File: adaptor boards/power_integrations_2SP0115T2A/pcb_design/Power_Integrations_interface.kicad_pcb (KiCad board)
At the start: 2 copper layers, 160 x 90 mm, 1042 parts, among them J1 GATE_DRIVER_CONN_U, J10 current sensor, J2 GATE_DRIVER_CONN_V, J3 GATE_DRIVER_CONN_W, J4 VBUS, J5 CONN-100MIL-F-1x2, J6 CONN-100MIL-M-1x4, J8 current sensor, J9 current sensor, P1 2SP0115T_conector, P2 2SP0115T_conector, P3 2SP0115T_conector, T1 TRANS-2CT, T2 TRANS-2CT, U1 LM1117IMP-v.v, U12 AMC1301, U2 SN6501DBV, U3 AMC1301, U4 TPS76350, U5 SN6501DBV, U6 AMC1301, U7 TPS76350, U9 AMC1301

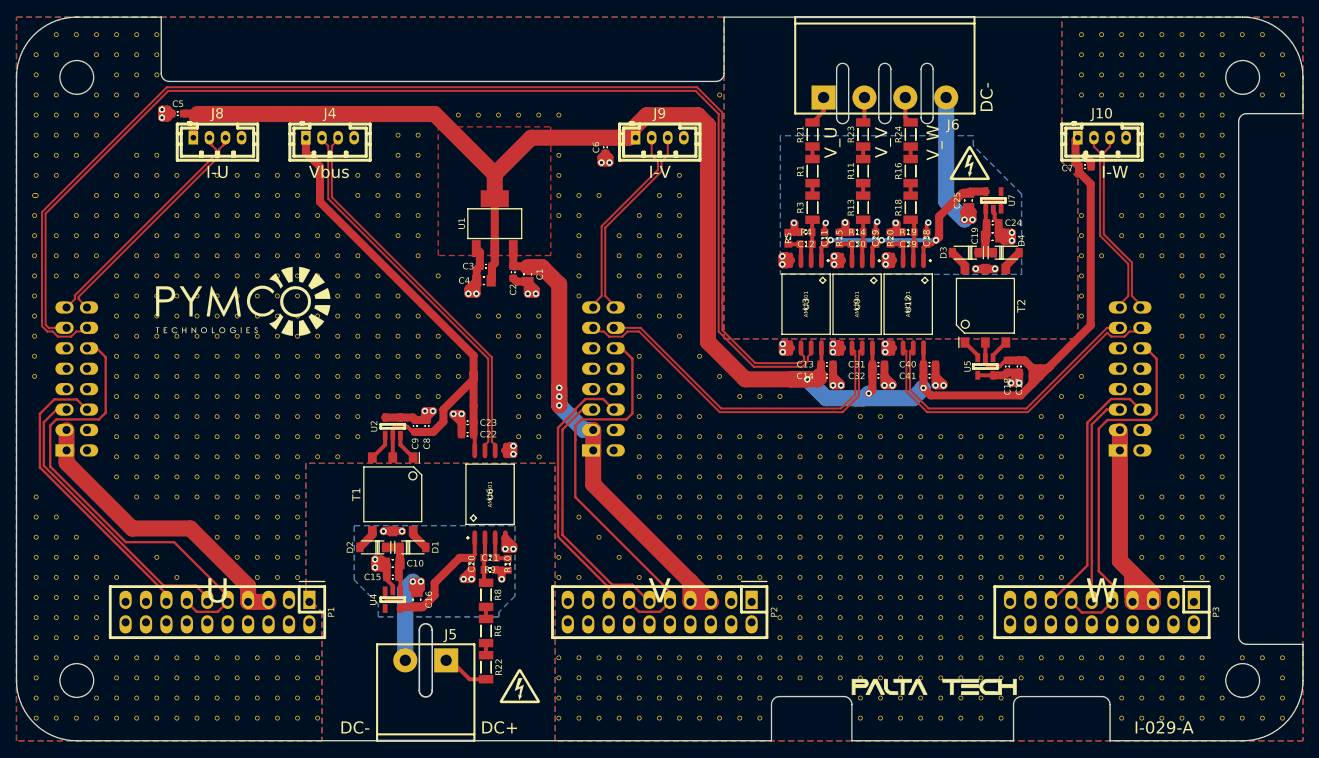
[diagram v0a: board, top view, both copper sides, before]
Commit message: Fix swapped differential signals in the interface board
Signed-off-by: Marcos Chaparro <mchaparro@paltatech.com>
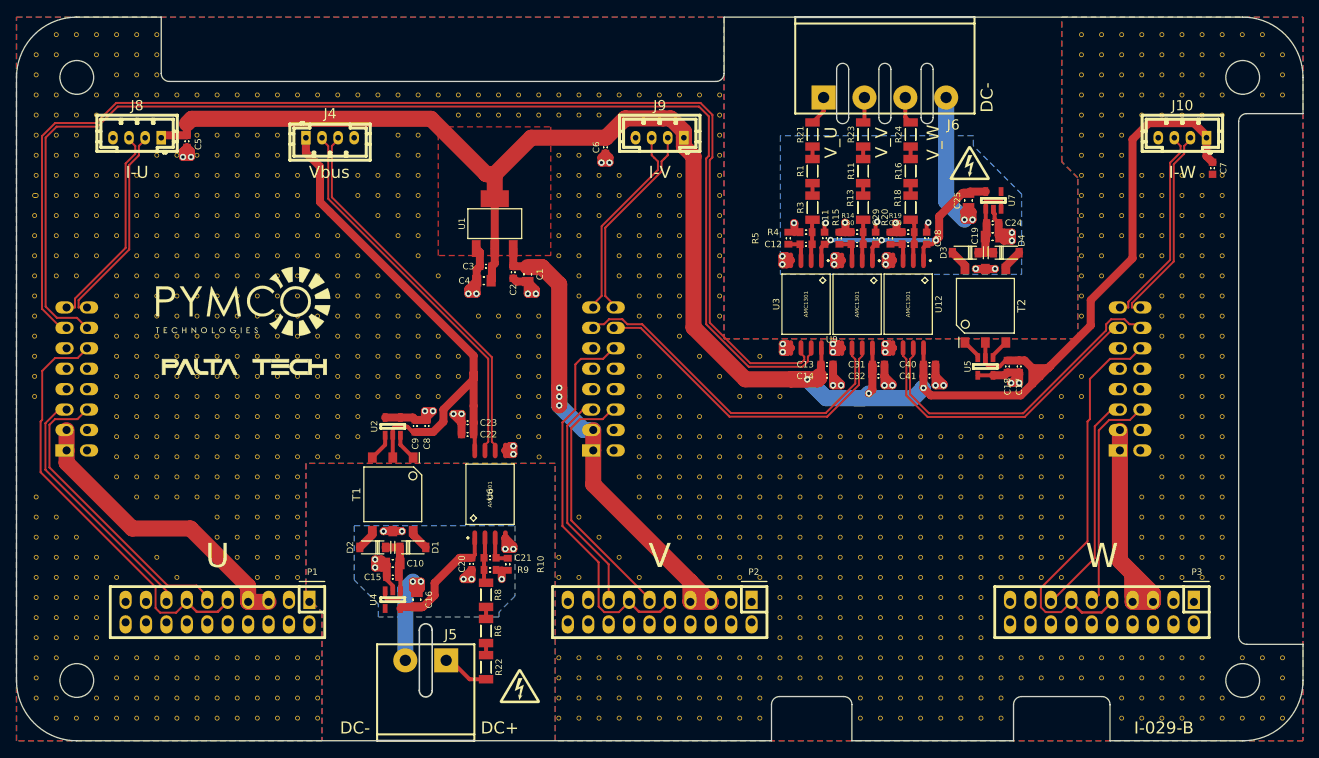
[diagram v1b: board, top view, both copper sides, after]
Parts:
- removed V1_35, V4_6, V5_5, V60_7, V6_7: AUTO_VIA, VIA_MATRIX
- added V10_17: AUTO_VIA, VIA_MATRIX, F.Cu at (-50.0, -35.3)
- added V10_17: AUTO_VIA, VIA_MATRIX, F.Cu at (-25.0, -35.3)
- added V10_8: AUTO_VIA, VIA_MATRIX, F.Cu at (-55.0, -30.3)
- added V10_9: AUTO_VIA, VIA_MATRIX, F.Cu at (-55.0, -27.8)
- added V11_17: AUTO_VIA, VIA_MATRIX, F.Cu at (-47.5, -35.3)
- added V11_17: AUTO_VIA, VIA_MATRIX, F.Cu at (-22.5, -35.3)
- added V11_8: AUTO_VIA, VIA_MATRIX, F.Cu at (-52.5, -30.3)
- added V11_9: AUTO_VIA, VIA_MATRIX, F.Cu at (-52.5, -27.8)
- added V12_17: AUTO_VIA, VIA_MATRIX, F.Cu at (-45.0, -35.3)
- added V12_17: AUTO_VIA, VIA_MATRIX, F.Cu at (-20.0, -35.3)
- added V12_8: AUTO_VIA, VIA_MATRIX, F.Cu at (-50.0, -30.3)
- added V12_9: AUTO_VIA, VIA_MATRIX, F.Cu at (-50.0, -27.8)
- added V13_17: AUTO_VIA, VIA_MATRIX, F.Cu at (-42.5, -35.3)
- added V13_17: AUTO_VIA, VIA_MATRIX, F.Cu at (-17.5, -35.3)
- added V13_8: AUTO_VIA, VIA_MATRIX, F.Cu at (-47.5, -30.3)
- added V13_9: AUTO_VIA, VIA_MATRIX, F.Cu at (-47.5, -27.8)
- added V14_17: AUTO_VIA, VIA_MATRIX, F.Cu at (-40.0, -35.3)
- added V14_17: AUTO_VIA, VIA_MATRIX, F.Cu at (-15.0, -35.3)
- added V15_17: AUTO_VIA, VIA_MATRIX, F.Cu at (-12.5, -35.3)
- added V16_17: AUTO_VIA, VIA_MATRIX, F.Cu at (-10.0, -35.3)
- added V17_17: AUTO_VIA, VIA_MATRIX, F.Cu at (-7.55, -35.3)
- added V18_17: AUTO_VIA, VIA_MATRIX, F.Cu at (-5.05, -35.3)
- added V19_17: AUTO_VIA, VIA_MATRIX, F.Cu at (-2.55, -35.3)
- added V1_8: AUTO_VIA, VIA_MATRIX, F.Cu at (-77.7, 2.18)
- added V20_17: AUTO_VIA, VIA_MATRIX, F.Cu at (-0.05, -35.3)
- added V21_17: AUTO_VIA, VIA_MATRIX, F.Cu at (2.45, -35.3)
- added V22_17: AUTO_VIA, VIA_MATRIX, F.Cu at (4.95, -35.3)
- added V26_5: AUTO_VIA, VIA_MATRIX, F.Cu at (-10.0, -32.8)
- added V27_10: AUTO_VIA, VIA_MATRIX, F.Cu at (-12.5, -15.3)
- added V27_5: AUTO_VIA, VIA_MATRIX, F.Cu at (-7.55, -32.8)
- added V27_7: AUTO_VIA, VIA_MATRIX, F.Cu at (-10.0, -27.8)
- added V27_9: AUTO_VIA, VIA_MATRIX, F.Cu at (-12.5, -17.8)
- added V28_10: AUTO_VIA, VIA_MATRIX, F.Cu at (-7.55, -20.3)
- added V28_9: AUTO_VIA, VIA_MATRIX, F.Cu at (-10.0, -25.3)
- added V29_9: AUTO_VIA, VIA_MATRIX, F.Cu at (-5.05, -25.3)
- added V29_9: AUTO_VIA, VIA_MATRIX, F.Cu at (-5.05, -22.8)
- added V29_9: AUTO_VIA, VIA_MATRIX, F.Cu at (-7.55, -25.3)
- added V2_11: AUTO_VIA, VIA_MATRIX, F.Cu at (-75.0, -20.3)
- added V33_10: AUTO_VIA, VIA_MATRIX, F.Cu at (7.45, -22.8)
- added V33_11: AUTO_VIA, VIA_MATRIX, F.Cu at (7.45, -20.3)
- added V33_12: AUTO_VIA, VIA_MATRIX, F.Cu at (7.45, -17.8)
- added V33_13: AUTO_VIA, VIA_MATRIX, F.Cu at (7.45, -15.3)
- added V33_14: AUTO_VIA, VIA_MATRIX, F.Cu at (7.45, -12.8)
- added V33_15: AUTO_VIA, VIA_MATRIX, F.Cu at (7.45, -10.3)
- added V33_16: AUTO_VIA, VIA_MATRIX, F.Cu at (7.45, -7.82)
- added V33_8: AUTO_VIA, VIA_MATRIX, F.Cu at (7.45, -32.8)
- added V33_8: AUTO_VIA, VIA_MATRIX, F.Cu at (7.45, -27.8)
- added V33_9: AUTO_VIA, VIA_MATRIX, F.Cu at (7.45, -30.3)
- added V33_9: AUTO_VIA, VIA_MATRIX, F.Cu at (7.45, -25.3)
- added V36_19: AUTO_VIA, VIA_MATRIX, F.Cu at (12.5, -2.82)
- added V3_10: AUTO_VIA, VIA_MATRIX, F.Cu at (-75.0, -22.8)
- added V4_10: AUTO_VIA, VIA_MATRIX, F.Cu at (-72.5, -25.3)
- added V4_10: AUTO_VIA, VIA_MATRIX, F.Cu at (-72.5, -22.8)
- added V4_9: AUTO_VIA, VIA_MATRIX, F.Cu at (-70.0, -25.3)
- added V53_4: AUTO_VIA, VIA_MATRIX, F.Cu at (52.5, -27.8)
- added V54_12: AUTO_VIA, VIA_MATRIX, F.Cu at (55.0, -12.8)
- added V54_4: AUTO_VIA, VIA_MATRIX, F.Cu at (55.0, -27.8)
- added V55_4: AUTO_VIA, VIA_MATRIX, F.Cu at (57.5, -27.8)
- added V56_12: AUTO_VIA, VIA_MATRIX, F.Cu at (60.0, -12.8)
- added V57_24: AUTO_VIA, VIA_MATRIX, F.Cu at (62.5, 9.68)
- added V57_25: AUTO_VIA, VIA_MATRIX, F.Cu at (62.5, 12.2)
- added V57_6: AUTO_VIA, VIA_MATRIX, F.Cu at (52.5, -25.3)
- added V57_7: AUTO_VIA, VIA_MATRIX, F.Cu at (52.5, -22.8)
- added V58_14: AUTO_VIA, VIA_MATRIX, F.Cu at (62.5, -10.3)
- added V58_15: AUTO_VIA, VIA_MATRIX, F.Cu at (62.5, -7.82)
- added V58_16: AUTO_VIA, VIA_MATRIX, F.Cu at (62.5, -5.32)
- added V58_6: AUTO_VIA, VIA_MATRIX, F.Cu at (55.0, -20.3)
- added V58_6: AUTO_VIA, VIA_MATRIX, F.Cu at (55.0, -25.3)
- added V58_7: AUTO_VIA, VIA_MATRIX, F.Cu at (55.0, -17.8)
- added V58_7: AUTO_VIA, VIA_MATRIX, F.Cu at (55.0, -22.8)
- added V59_6: AUTO_VIA, VIA_MATRIX, F.Cu at (57.5, -25.3)
- added V59_7: AUTO_VIA, VIA_MATRIX, F.Cu at (57.5, -22.8)
- added V6_12: AUTO_VIA, VIA_MATRIX, F.Cu at (-65.0, -17.8)
- added V6_17: AUTO_VIA, VIA_MATRIX, F.Cu at (-60.0, -35.3)
- added V6_17: AUTO_VIA, VIA_MATRIX, F.Cu at (-62.5, -35.3)
- added V6_17: AUTO_VIA, VIA_MATRIX, F.Cu at (-37.5, -35.3)
- added V6_17: AUTO_VIA, VIA_MATRIX, F.Cu at (-35.0, -35.3)
- added V7_11: AUTO_VIA, VIA_MATRIX, F.Cu at (-62.5, -20.3)
- added V7_17: AUTO_VIA, VIA_MATRIX, F.Cu at (-57.5, -35.3)
- added V7_17: AUTO_VIA, VIA_MATRIX, F.Cu at (-32.5, -35.3)
- added V8_10: AUTO_VIA, VIA_MATRIX, F.Cu at (-60.0, -27.8)
- added V8_10: AUTO_VIA, VIA_MATRIX, F.Cu at (-60.0, -22.8)
- added V8_17: AUTO_VIA, VIA_MATRIX, F.Cu at (-55.0, -35.3)
- added V8_17: AUTO_VIA, VIA_MATRIX, F.Cu at (-30.0, -35.3)
- added V9_17: AUTO_VIA, VIA_MATRIX, F.Cu at (-52.5, -35.3)
- added V9_17: AUTO_VIA, VIA_MATRIX, F.Cu at (-27.5, -35.3)
- added V9_9: AUTO_VIA, VIA_MATRIX, F.Cu at (-57.5, -30.3)
- added V9_9: AUTO_VIA, VIA_MATRIX, F.Cu at (-57.5, -27.8)
- added V9_9: AUTO_VIA, VIA_MATRIX, F.Cu at (-57.5, -25.3)
- C1, C4: value 10uF -> 22uF
- J6: value CONN-100MIL-M-1x4 -> Phoenix 1757268 5.08mm
- R1, R11, R13, R16, R18, R21, R22, R23, R24, R3, R6, R8: value 1M -> 500k
- moved G*** 94.6 mm to (-51.8, -1.50)
- moved C7 15.9 mm to (68.8, -26.2), turned to 270 degrees
- moved V57_6 10.3 mm to (52.5, -32.8)
- moved V57_7 10.3 mm to (52.5, -30.3)
- moved V58_6 10.3 mm to (55.0, -32.8)
- moved V58_7 10.3 mm to (55.0, -30.3)
- moved V59_6 10.3 mm to (57.5, -32.8)
- moved V59_7 10.3 mm to (57.5, -30.3)
- moved V60_6 10.3 mm to (60.0, -32.8)
- moved J10 10.0 mm to (65.0, -30.0), turned to 180 degrees
- moved J8 10.0 mm to (-65.0, -30.0), turned to 180 degrees
- moved C5 3.64 mm to (-58.8, -29.6), turned to 270 degrees
- turned J9 to 180 degrees
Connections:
- J1 pad 13: /V_phase_U/Vout+ -> /V_phase_U/Vout-
- J1 pad 14: /V_phase_U/Vout- -> /V_phase_U/Vout+
- J1 pad 15: /I_phase_U+ -> /I_phase_U-
- J1 pad 16: /I_phase_U- -> /I_phase_U+
- J2 pad 13: /V_phase_V/Vout+ -> /V_phase_V/Vout-
- J2 pad 14: /V_phase_V/Vout- -> /V_phase_V/Vout+
- J2 pad 15: /I_phase_V+ -> /I_phase_V-
- J2 pad 16: /I_phase_V- -> /I_phase_V+
- J3 pad 13: /V_phase_W/Vout+ -> /V_phase_W/Vout-
- J3 pad 14: /V_phase_W/Vout- -> /V_phase_W/Vout+
- J3 pad 15: /I_phase_W+ -> /I_phase_W-
- J3 pad 16: /I_phase_W- -> /I_phase_W+
- P1 pad 11: Net-(J1-Pad5) -> Net-(J1-Pad6)
- P1 pad 15: Net-(J1-Pad6) -> Net-(J1-Pad5)
- P2 pad 11: Net-(J2-Pad5) -> Net-(J2-Pad6)
- P2 pad 15: Net-(J2-Pad6) -> Net-(J2-Pad5)
- P3 pad 11: Net-(J3-Pad5) -> Net-(J3-Pad6)
- P3 pad 15: Net-(J3-Pad6) -> Net-(J3-Pad5)
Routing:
- net +5: track 235.4 -> 244.8 mm
- net /V_phase_U/Vout+: track 149.9 -> 155.4 mm
- net /V_phase_W/Vout+: track 36.6 -> 41.9 mm
- net /I_phase_U+: track 30.4 -> 25.6 mm
- net /I_phase_U-: track 30.3 -> 25.6 mm
- net Net-(J3-Pad6): track 32.5 -> 27.9 mm
- net ~FAULT_W: track 45.8 -> 50.2 mm
- net /V_phase_V/Vout-: track 40.9 -> 44.6 mm
- net /V_phase_V/Vout+: track 44.8 -> 41.9 mm
- net ~FAULT_U: track 57.9 -> 55.0 mm
- net Net-(J2-Pad5): track 32.3 -> 29.5 mm
- net Net-(J1-Pad5): track 36.6 -> 34.0 mm
- net /I_phase_W-: track 23.3 -> 25.5 mm
- net /I_phase_W+: track 23.3 -> 25.5 mm
- net Net-(J3-Pad5): track 26.3 -> 28.1 mm
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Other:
- board text added: "I-029-B"
- board text removed: "I-029-A"
